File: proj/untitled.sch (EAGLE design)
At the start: 64 parts, among them J1 SPKRAST_01532MR, J2 MICCMA-4544PF-W, J3 ADAFRUIT_OLED_13, U1 SIM5300EA, U10 3.3V 600mA, U2 MIC29302TO-263-5, U3 MCP23008QFN, U4 MCP23008QFN, U5 MCP23008QFN, U6 TXB0108, U7 SN74LVC1G125SOT23-5, U8 USIM_CONN, U9 ESDA6V1-5W6

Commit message: Completed mobile phone (untitled) schematic Started routing mobile phone board
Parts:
- added C25, C26, C30, C31, C42: 10uF, dooba:CAP0805
- added C27, C28, C29, C32, C35, C36, C37, C38, C39, C45: 100nF, dooba:CAP0805
- added C33, C34: 27pF, dooba:CAP0805
- added C40: 470pF, dooba:CAP0805
- added C41: 4.7nF, dooba:CAP0805
- added C43, C44: 3.3uF, dooba:CAP0805
- added C46, C47: 3.3nF, dooba:CAP0805
- added C48, C51, C52, C53: 1uF, dooba:CAP0805
- added C49, C50: 100uF, dooba:CAP1210
- added J4: DM3D-SFDM, dooba:DM3D-SFDM
- added J5: SJ1-3523N, dooba:SJ1-3523N
- added J6: CONUFL001, dooba:CONUFL001
- added L1: 4.7uH, dooba:IND2520
- added R10, R14, R20: 10k, dooba:RES0805
- added R11: 1M, dooba:RES0805
- added R12, R13: 4.7R, dooba:RES0805
- added R15: 1k, dooba:RES0805
- added R16, R17: 560R, dooba:RES0805
- added R18, R19: 270k, dooba:RES0805
- added R22: 100k, dooba:RES0805
- added S1: SWITCH_SPDT, dooba:SWITCH_SPDT
- added U11: MCP1642B, dooba:MCP1642B
- added U12: STA013LQFP44, dooba:STA013LQFP44
- added U13: CS4334, dooba:CS4334
- added U14: LM4811PDSO-10, dooba:LM4811PDSO-10
- added X2: 14.7456MHz, dooba:XTAL_GNDSMD_3225
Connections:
- new net !STA013_RST: N1.PC2, R14.1, U12.!RESET
- new net 5.0V: C23.2, C26.2, C3.1, C30.1, C4.1, C42.2, C45.1, J3.VIN, N1.VIN@16, N1.VUSB@2, U10.EN, U10.VIN, U11.VOUT, U13.VA, U2.VIN, U7.VCC
- new net AMP_SHUTDOWN: N1.PC7, R22.1, U14.SHUTDOWN
- new net AMP_VOL_CLK: N1.PC6, U14.CLOCK
- new net AMP_VOL_UPDN: N1.PC5, U14.UP/DN
- new net AOUT_L: C46.1, C52.1, R17.2
- new net AOUT_R: C47.2, C53.1, R16.2
- new net I2C_SCL: J3.CLK, N1.PC0/SCL, R10.1, U12.SCL, U3.SCL, U4.SCL, U5.SCL
- new net I2C_SDA: J3.DATA, N1.PC1/SDA, R20.1, U12.SDA, U3.SDA, U4.SDA, U5.SDA
- new net MICROSD_CS: J4.DAT3/CS, N1.PA4/ADC4
- new net N$35: C34.2, R11.1, U12.XTI, X2.1
- new net N$40: C33.2, R11.2, U12.XTO, X2.2
- new net N$41: L1.2, U11.SW
- new net N$42: C39.1, R13.2, U12.PVDD
- new net N$45: C39.2, R12.1, U12.PVSS
- new net N$46: C41.2, R15.2
- new net N$49: C40.2, R15.1, U12.FILT
- new net N$50: C43.2, R18.1, U13.AOUTL
- new net N$51: C44.2, R19.2, U13.AOUTR
- new net N$52: C44.1, R16.1
- new net N$53: C43.1, R17.1
- new net N$54: C49.2, U14.VOUT1
- new net N$55: C50.2, U14.VOUT2
- new net N$56: C51.2, U14.BYPASS
- new net N$57: C50.1, J5.RING
- new net N$58: C52.2, U14.VIN1
- new net N$59: C53.2, U14.VIN2
- new net N$60: C49.1, J5.TIP
- new net N$61: J6.SIG, U1.RF_ANT
- new net SPI_MISO: J4.DAT0/DO, N1.MISO
- new net SPI_MOSI: J4.CMD/DI, N1.MOSI, U12.SDI
- new net SPI_SCK: J4.CLK/SCK, N1.SCK, U12.SCKR
- new net STA013_BIT_EN: N1.PC4, U12.BIT_EN
- new net STA013_DREQ: N1.PC3, U12.OUT_CLK/DATA_REC
- new net STA013_LRCKT: U12.LRCKT, U13.LRCK
- new net STA013_OCLK: U12.OCLK, U13.MCLK
- new net STA013_SCKT: U12.SCKT, U13.DEM/SCLK
- new net STA013_SDO: U12.SDO, U13.SDATA
- new net VBAT: S1.1
- net 3.3V: now also C27.2, C28.2, C29.1, C31.1, C32.1, C35.2, C36.2, C37.2, C38.2, C48.2, J4.VCC, R10.2, R13.1, R14.2, R20.2, R22.2, U12.!SRC_INT, U12.!TESTEN, U12.VDD_1, U12.VDD_2, U12.VDD_3, U12.VDD_4, U14.VCC, U3.!RST, U3.A2, U3.VCC, U4.!RST, U4.A0, U4.A2, U4.VCC, U5.!RST, U5.A1, U5.A2, U5.VCC
- net GND: now also B1.2, B10.2, B11.2, B12.2, B13.COMMON, B13.GND1, B13.GND2, B14.1, B15.2, B16.1, B17.2, B2.2, B3.2, B4.2, B5.2, B6.2, B7.2, B8.2, B9.2, C25.2, C26.1, C27.1, C28.1, C29.2, C30.2, C31.2, C32.2, C33.1, C34.1, C35.1, C36.1, C37.1, C38.1, C40.1, C41.1, C42.1, C45.2, C46.2, C47.1, C48.1, C51.1, J3.GND, J4.GND, J4.GND_1, J4.GND_2, J4.GND_3, J4.GND_4, J5.SLEEVE, J6.GND@1, J6.GND@2, N1.GND, N1.GND@1, N1.GND@15, R12.2, R18.2, R19.1, U11.PGND, U11.SGND, U12.SCANEN, U12.VSS_1, U12.VSS_2, U12.VSS_3, U12.VSS_4, U12.VSS_5, U13.AGND, U14.GND, U3.A0, U3.A1, U3.GND, U3.PAD, U4.A1, U4.GND, U4.PAD, U5.A0, U5.GND, U5.PAD, X2.GND0, X2.GND1
- net GSM_PWR_EN: now also N1.PA0/ADC0
- net GSM_PWR_KEY: now also N1.PA1/ADC1
- net GSM_RING: now also N1.PA3/ADC3
- net GSM_RXD: now also N1.PD3/TXD1
- net GSM_STATUS: now also N1.PA2/ADC2
- net GSM_TXD: now also N1.PD2/RXD1
- net VIN: now also C25.1, L1.1, S1.2, U11.EN, U11.VIN; no longer C23.2, C3.1, C4.1, U10.EN, U10.VIN, U2.VIN, U7.VCC
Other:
- note added: "3.3V Power Supply"
- note added: "5.0V Boost Converter"
- note added: "Audio DAC"
- note added: "Core Control (ioNode)"
- note added: "GSM Power Supply"
- note added: "GSM Subsystem"
- note added: "Headphone Amplifier"
- note added: "I2C Bus Pullups"
- note added: "MP3 Decoder"
- note added: "MP3 Player Subsystem"
- note added: "MicroSD Connector"
- note added: "Misc"
- note added: "Power Supplies"
- note added: "User Interface"
- moved on the sheet: B1, B10, B11, B12, B13, B14, B15, B16, B17, B2, B3, B4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

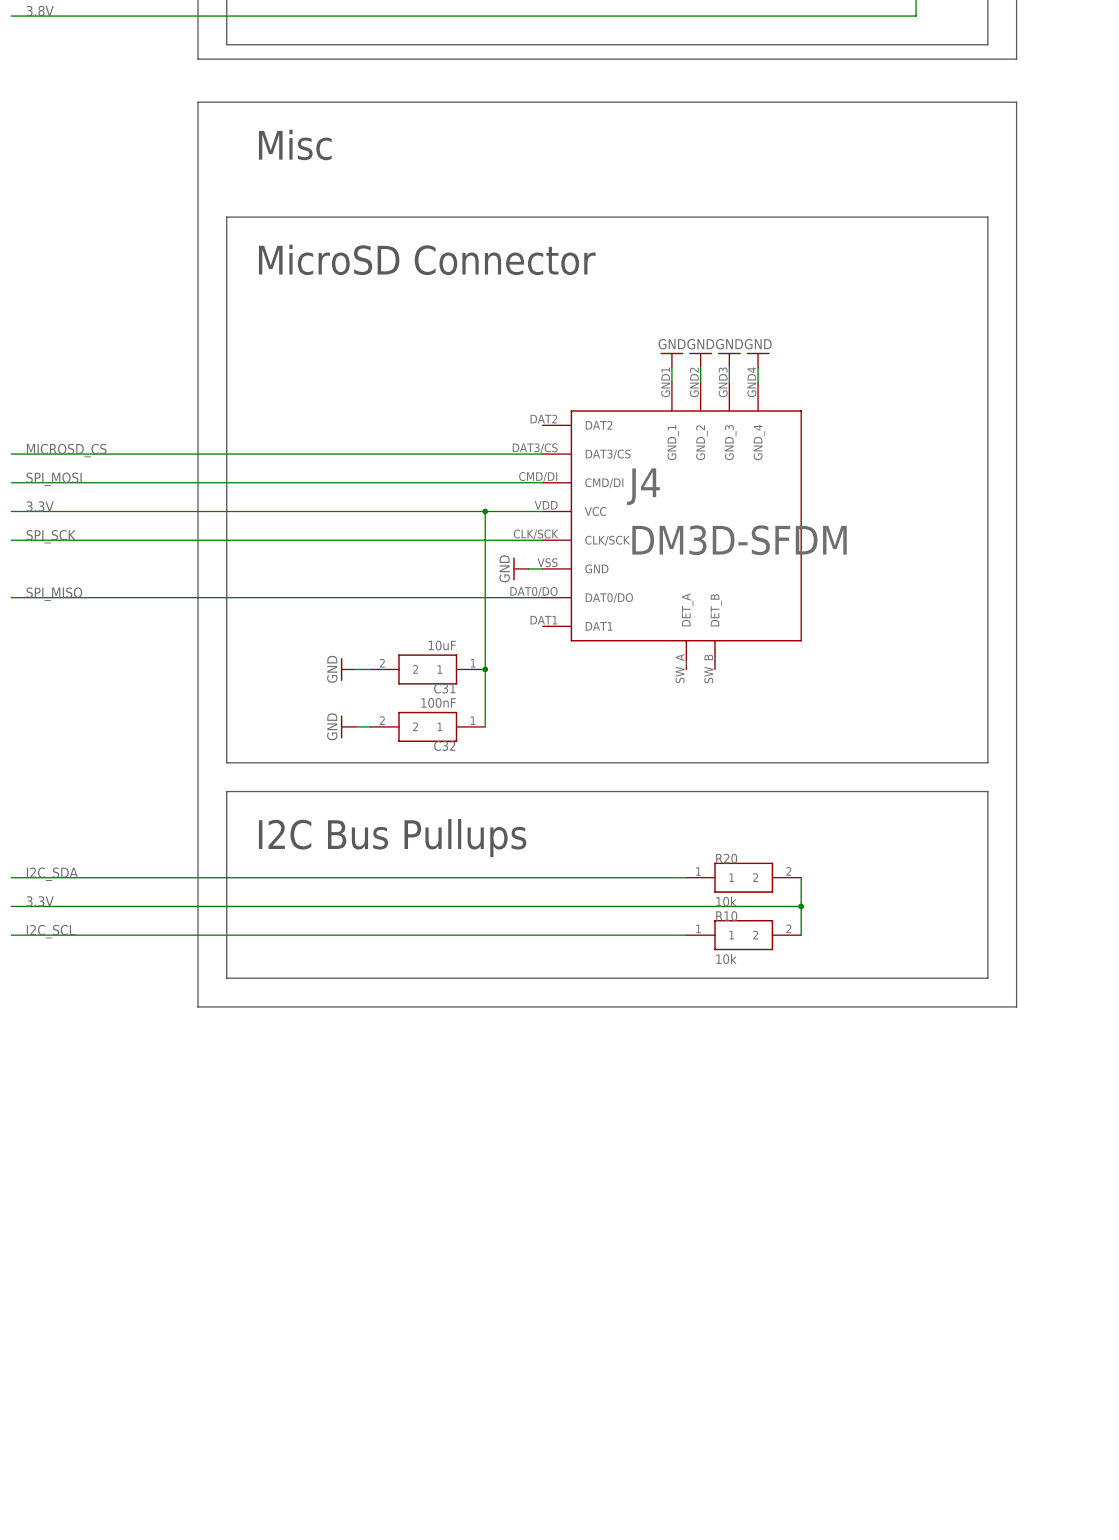
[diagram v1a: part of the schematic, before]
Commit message: Added Z3OC Vibration Motor to Eagle Library Added Vibrator to mobile phone schematic
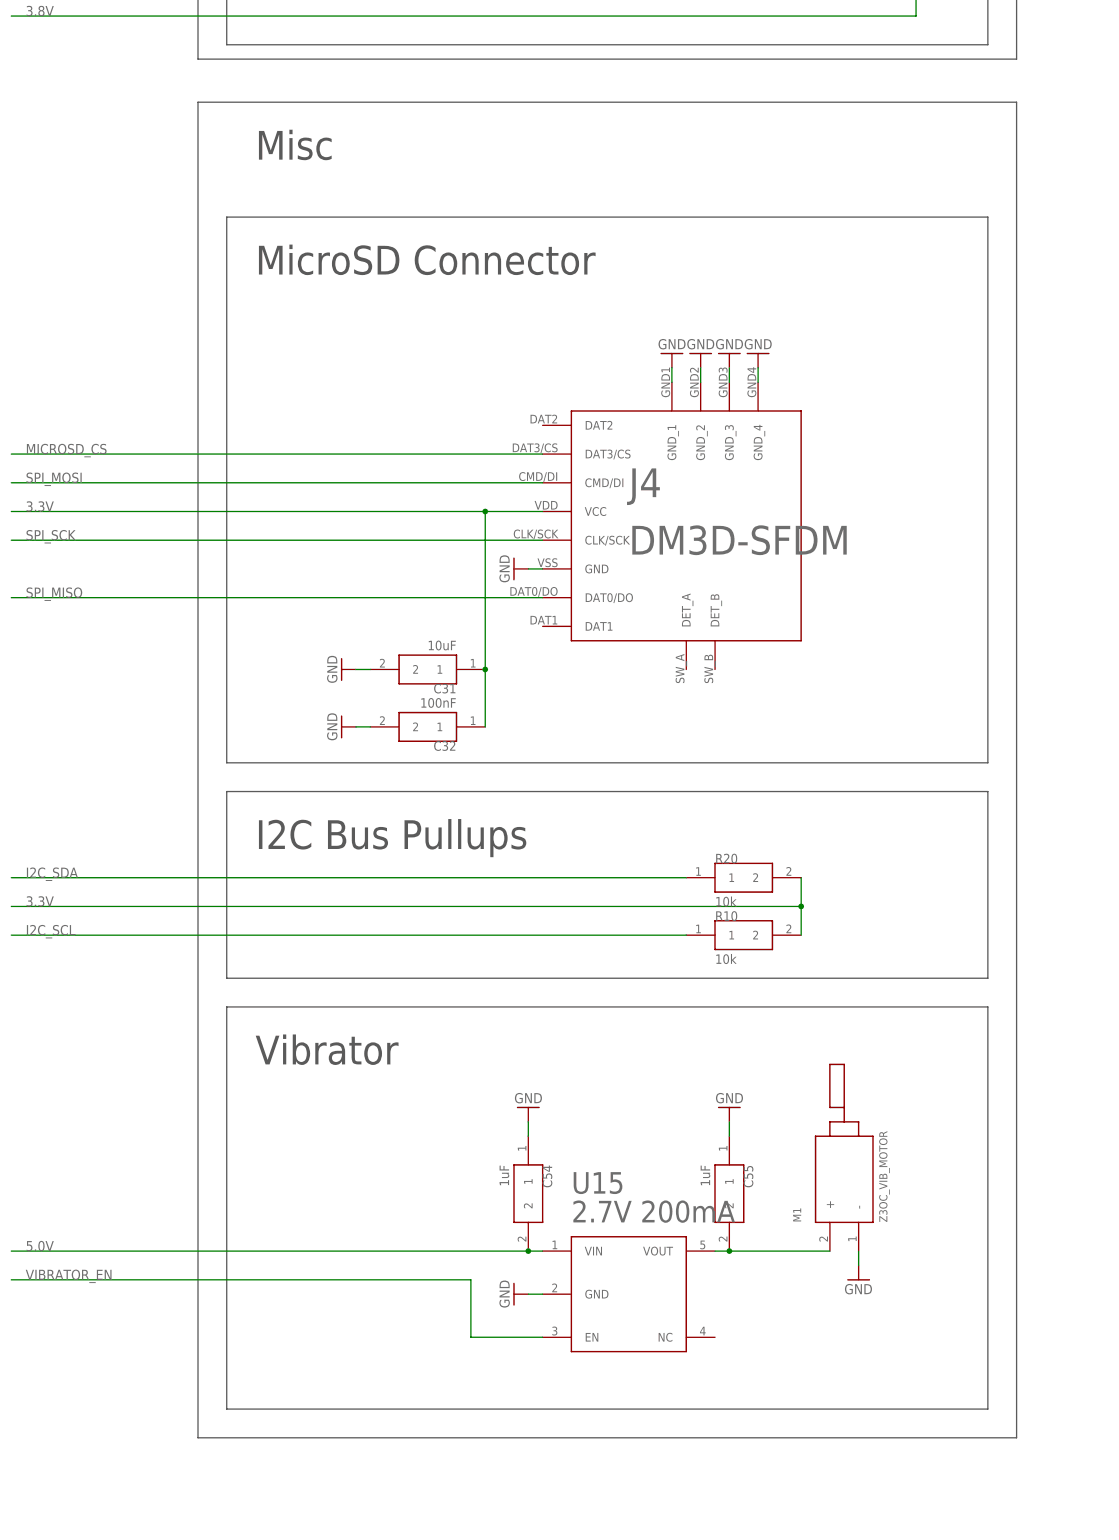
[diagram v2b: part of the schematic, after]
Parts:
- added C54, C55: 1uF, dooba:CAP0805
- added M1: Z3OC_VIB_MOTOR, dooba:Z3OC_VIB_MOTOR
- added U15: 2.7V 200mA, dooba:LP3985SOT23-5
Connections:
- new net 2.7V: C55.2, M1.+, U15.VOUT
- new net VIBRATOR_EN: U15.EN
- net 5.0V: now also C54.2, U15.VIN
- net GND: now also C54.1, C55.1, M1.-, U15.GND
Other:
- note added: "Vibrator"
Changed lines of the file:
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@@
 <part name="GND127" library="supply1" library_urn="urn:adsk.eagle:library:371" deviceset="GND" device=""/>
 <part name="GND128" library="supply1" library_urn="urn:adsk.eagle:library:371" deviceset="GND" device=""/>
+<part name="M1" library="dooba" deviceset="Z3OC_VIB_MOTOR" device=""/>
+<part name="U15" library="dooba" deviceset="LP3985" device="SOT23-5" value="2.7V 200mA"/>
+<part name="C54" library="dooba" deviceset="CAP" device="0805" value="1uF"/>
+<part name="C55" library="dooba" deviceset="CAP" device="0805" value="1uF"/>
+<part name="GND129" library="supply1" library_urn="urn:adsk.eagle:library:371" deviceset="GND" device=""/>
+<part name="GND130" library="supply1" library_urn="urn:adsk.eagle:library:371" deviceset="GND" device=""/>
+<part name="GND131" library="supply1" library_urn="urn:adsk.eagle:library:371" deviceset="GND" device=""/>
+<part name="GND132" library="supply1" library_urn="urn:adsk.eagle:library:371" deviceset="GND" device=""/>
 </parts>
 <sheets>
@@
 <text x="25.4" y="508" size="5.08" layer="97">Misc</text>
 <wire x1="15.24" y1="518.16" x2="160.02" y2="518.16" width="0.1524" layer="97"/>
-<wire x1="160.02" y1="518.16" x2="160.02" y2="358.14" width="0.1524" layer="97"/>
-<wire x1="160.02" y1="358.14" x2="15.24" y2="358.14" width="0.1524" layer="97"/>
-<wire x1="15.24" y1="358.14" x2="15.24" y2="518.16" width="0.1524" layer="97"/>
+<wire x1="160.02" y1="518.16" x2="160.02" y2="281.94" width="0.1524" layer="97"/>
+<wire x1="160.02" y1="281.94" x2="15.24" y2="281.94" width="0.1524" layer="97"/>
+<wire x1="15.24" y1="281.94" x2="15.24" y2="518.16" width="0.1524" layer="97"/>
+<wire x1="20.32" y1="358.14" x2="154.94" y2="358.14" width="0.1524" layer="97"/>
+<wire x1="154.94" y1="358.14" x2="154.94" y2="287.02" width="0.1524" layer="97"/>
+<wire x1="154.94" y1="287.02" x2="20.32" y2="287.02" width="0.1524" layer="97"/>
+<wire x1="20.32" y1="287.02" x2="20.32" y2="358.14" width="0.1524" layer="97"/>
+<text x="25.4" y="347.98" size="5.08" layer="97">Vibrator</text>
 </plain>
 <instances>
@@
 <instance part="GND127" gate="1" x="744.22" y="800.1" rot="R180"/>
 <instance part="GND128" gate="1" x="744.22" y="769.62"/>
+<instance part="M1" gate="M1" x="129.54" y="322.58" rot="R90"/>
+<instance part="U15" gate="U1" x="91.44" y="307.34"/>
+<instance part="C54" gate="C1" x="73.66" y="325.12" rot="R270"/>
+<instance part="C55" gate="C1" x="109.22" y="325.12" rot="R270"/>
+<instance part="GND129" gate="1" x="71.12" y="307.34" rot="R270"/>
+<instance part="GND130" gate="1" x="73.66" y="340.36" rot="R180"/>
+<instance part="GND131" gate="1" x="109.22" y="340.36" rot="R180"/>
+<instance part="GND132" gate="1" x="132.08" y="309.88"/>
 </instances>
 <busses>
@@
 <wire x1="744.22" y1="772.16" x2="744.22" y2="774.7" width="0.1524" layer="91"/>
 </segment>
+<segment>
+<pinref part="U15" gate="U1" pin="GND"/>
+<pinref part="GND129" gate="1" pin="GND"/>
+<wire x1="73.66" y1="307.34" x2="76.2" y2="307.34" width="0.1524" layer="91"/>
+</segment>
+<segment>
+<pinref part="C54" gate="C1" pin="1"/>
+<pinref part="GND130" gate="1" pin="GND"/>
+<wire x1="73.66" y1="337.82" x2="73.66" y2="335.28" width="0.1524" layer="91"/>
+</segment>
+<segment>
+<pinref part="C55" gate="C1" pin="1"/>
+<pinref part="GND131" gate="1" pin="GND"/>
+<wire x1="109.22" y1="337.82" x2="109.22" y2="335.28" width="0.1524" layer="91"/>
+</segment>
+<segment>
+<pinref part="M1" gate="M1" pin="-"/>
+<pinref part="GND132" gate="1" pin="GND"/>
+<wire x1="132.08" y1="312.42" x2="132.08" y2="314.96" width="0.1524" layer="91"/>
+</segment>
 </net>
 <net name="N$28" class="0">
@@
 <junction x="66.04" y="662.94"/>
 </segment>
+<segment>
+<pinref part="U15" gate="U1" pin="VIN"/>
+<pinref part="C54" gate="C1" pin="2"/>
+<wire x1="76.2" y1="314.96" x2="73.66" y2="314.96" width="0.1524" layer="91"/>
+<junction x="73.66" y="314.96"/>
+<label x="-15.24" y="314.96" size="1.778" layer="95"/>
+<wire x1="73.66" y1="314.96" x2="-17.78" y2="314.96" width="0.1524" layer="91"/>
+</segment>
 </net>
 <net name="VIN" class="0">
@@
 </segment>
 </net>
+<net name="2.7V" class="0">
+<segment>
+<pinref part="U15" gate="U1" pin="VOUT"/>
+<pinref part="C55" gate="C1" pin="2"/>
+<wire x1="106.68" y1="314.96" x2="109.22" y2="314.96" width="0.1524" layer="91"/>
+<pinref part="M1" gate="M1" pin="+"/>
+<wire x1="109.22" y1="314.96" x2="127" y2="314.96" width="0.1524" layer="91"/>
+<junction x="109.22" y="314.96"/>
+</segment>
+</net>
+<net name="VIBRATOR_EN" class="0">
+<segment>
+<pinref part="U15" gate="U1" pin="EN"/>
+<wire x1="76.2" y1="299.72" x2="63.5" y2="299.72" width="0.1524" layer="91"/>
+<wire x1="63.5" y1="299.72" x2="63.5" y2="309.88" width="0.1524" layer="91"/>
+<wire x1="63.5" y1="309.88" x2="-17.78" y2="309.88" width="0.1524" layer="91"/>
+<label x="-15.24" y="309.88" size="1.778" layer="95"/>
+</segment>
+</net>

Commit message: Further routed mobile phone board
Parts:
- added BAT[+-]: PIN_2, dooba:PIN_2
- added R23: 10k, dooba:RES0805
- added U16: SN74LVC1G125SOT23-5, dooba:SN74LVC1G125SOT23-5
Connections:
- new net N$62: U15.EN, U16.Y
- net 5.0V: now also U16.VCC
- net GND: now also BAT[+-].2, R23.2, U16.!OE, U16.GND
- net GSM_PWR_KEY: now also N1.PA2/ADC2; no longer N1.PA1/ADC1
- net GSM_RING: now also N1.PA1/ADC1; no longer N1.PA3/ADC3
- net GSM_STATUS: now also N1.PA3/ADC3; no longer N1.PA2/ADC2
- net N$18: now also B4.1; no longer B7.1
- net N$19: now also B7.1; no longer B4.1
- net VBAT: now also BAT[+-].1
- net VIBRATOR_EN: now also N1.PB3, R23.1, U16.A; no longer U15.EN
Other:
- moved on the sheet: B4, B7, C54, C55, M1, S1, U15

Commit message: Further routed mobile phone board
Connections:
- net 5.0V: no longer N1.VUSB@2
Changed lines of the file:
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@@
 </segment>
 <segment>
-<pinref part="N1" gate="N1" pin="VUSB@2"/>
-<wire x1="302.26" y1="434.34" x2="292.1" y2="434.34" width="0.1524" layer="91"/>
 <pinref part="N1" gate="N1" pin="VIN@16"/>
 <wire x1="292.1" y1="434.34" x2="185.42" y2="434.34" width="0.1524" layer="91"/>
@@
 <wire x1="360.68" y1="447.04" x2="292.1" y2="447.04" width="0.1524" layer="91"/>
 <wire x1="292.1" y1="447.04" x2="292.1" y2="434.34" width="0.1524" layer="91"/>
-<junction x="292.1" y="434.34"/>
 <label x="187.96" y="434.34" size="1.778" layer="95"/>
 </segment>
